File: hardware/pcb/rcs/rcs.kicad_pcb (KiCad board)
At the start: 2 copper layers, 66 x 46 mm, 28 parts, among them J1 UART, Q1 BS170, Q2 BS170, Q3 BS170, Q4 BS170, Q5 BS170, Q6 BS170, U1 ESP32

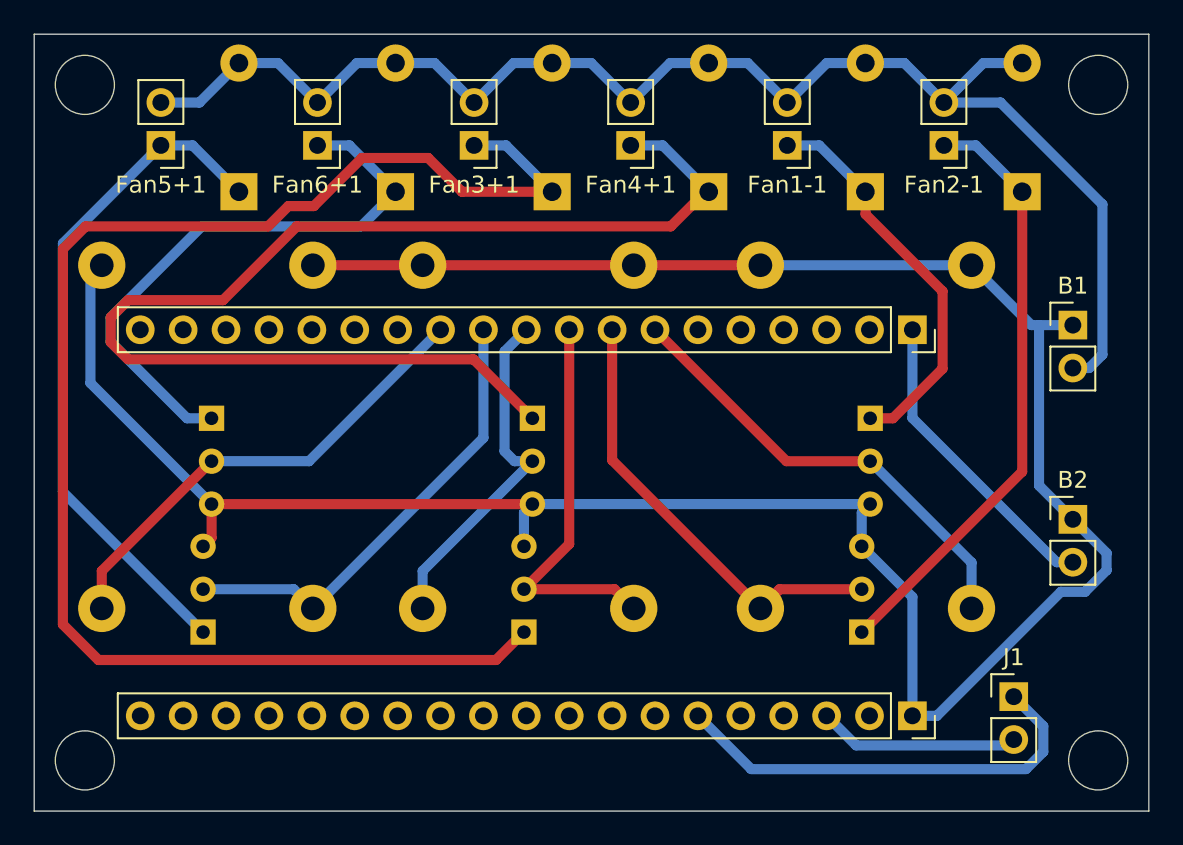
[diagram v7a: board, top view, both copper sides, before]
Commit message: Fix flyback diode orientation, round pcb corners
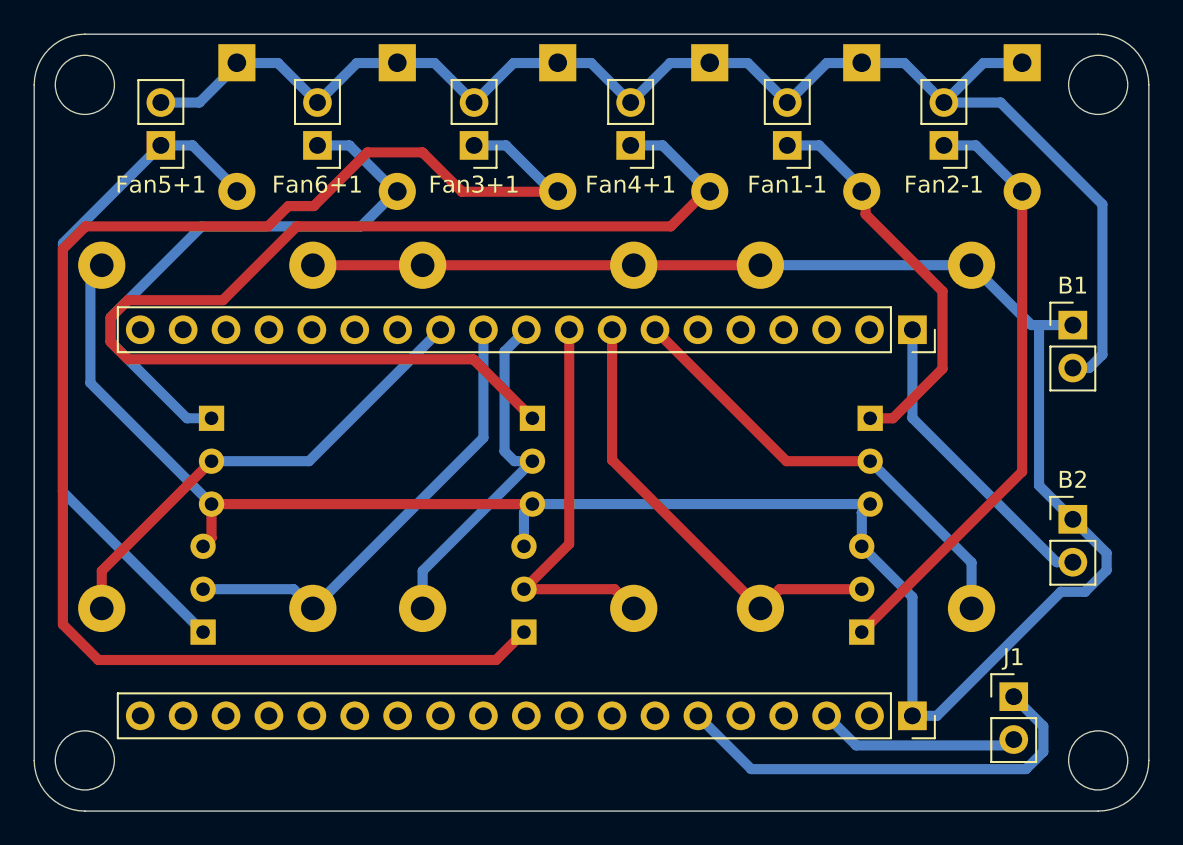
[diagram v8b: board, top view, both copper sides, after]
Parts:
- moved D5 47.1 mm to (173.0, 48.2), turned to -90 degrees
- moved D2 47.0 mm to (219.5, 48.2), turned to -90 degrees
- moved D6 28.7 mm to (182.5, 48.2), turned to -90 degrees
- moved D1 28.6 mm to (210.0, 48.2), turned to -90 degrees
- moved D4 12.1 mm to (201.0, 48.2), turned to -90 degrees
- moved D3 11.8 mm to (192.0, 48.2), turned to -90 degrees
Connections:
- D1 pad 1: Net-(D1-K) -> +15V
- D1 pad 2: +15V -> Net-(D1-A)
- D2 pad 1: Net-(D2-K) -> +15V
- D2 pad 2: +15V -> Net-(D2-A)
- D3 pad 1: Net-(D3-K) -> +15V
- D3 pad 2: +15V -> Net-(D3-A)
- D4 pad 1: Net-(D4-K) -> +15V
- D4 pad 2: +15V -> Net-(D4-A)
- D5 pad 1: Net-(D5-K) -> +15V
- D5 pad 2: +15V -> Net-(D5-A)
- D6 pad 1: Net-(D6-K) -> +15V
- D6 pad 2: +15V -> Net-(D6-A)
- Fan1-1 pad 1: Net-(D1-K) -> Net-(D1-A)
- Fan2-1 pad 1: Net-(D2-K) -> Net-(D2-A)
- Fan3+1 pad 1: Net-(D3-K) -> Net-(D3-A)
- Fan4+1 pad 1: Net-(D4-K) -> Net-(D4-A)
- Fan5+1 pad 1: Net-(D5-K) -> Net-(D5-A)
- Fan6+1 pad 1: Net-(D6-K) -> Net-(D6-A)
- Q1 pad 1: Net-(D1-K) -> Net-(D1-A)
- Q2 pad 1: Net-(D2-K) -> Net-(D2-A)
- Q3 pad 1: Net-(D3-K) -> Net-(D3-A)
- Q4 pad 1: Net-(D4-K) -> Net-(D4-A)
- Q5 pad 1: Net-(D5-K) -> Net-(D5-A)
- Q6 pad 1: Net-(D6-K) -> Net-(D6-A)
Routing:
- net Net-(D3-A): track 0.00 -> 89.2 mm
- net Net-(D3-K): track 88.9 -> 0.00 mm
- net Net-(D4-K): track 72.7 -> 0.00 mm
- net Net-(D4-A): track 0.00 -> 72.7 mm
- net Net-(D5-K): track 40.4 -> 0.00 mm
- net Net-(D5-A): track 0.00 -> 40.4 mm
- net Net-(D2-K): track 36.0 -> 0.00 mm
- net Net-(D2-A): track 0.00 -> 36.0 mm
- net Net-(D6-K): track 35.0 -> 0.00 mm
- net Net-(D6-A): track 0.00 -> 35.0 mm
- net Net-(D1-K): track 23.8 -> 0.00 mm
- net Net-(D1-A): track 0.00 -> 23.8 mm
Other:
- outline, holes or cut-outs redrawn
